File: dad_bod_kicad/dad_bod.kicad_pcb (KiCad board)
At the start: 2 copper layers, 98.5 x 71.3 mm, 136 parts, among them J1 Conn_01x01, J10 Conn_01x03_Male, J11 BNC5-J-P-GN-RA-BH2D, J12 USB4085-GF-A_REVA4, J13 Conn_01x03_Male, J14 Conn_01x03_Male, J2 Conn_01x01, J3 Conn_01x01, J4 Conn_01x01, J5 Conn_01x03_Male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

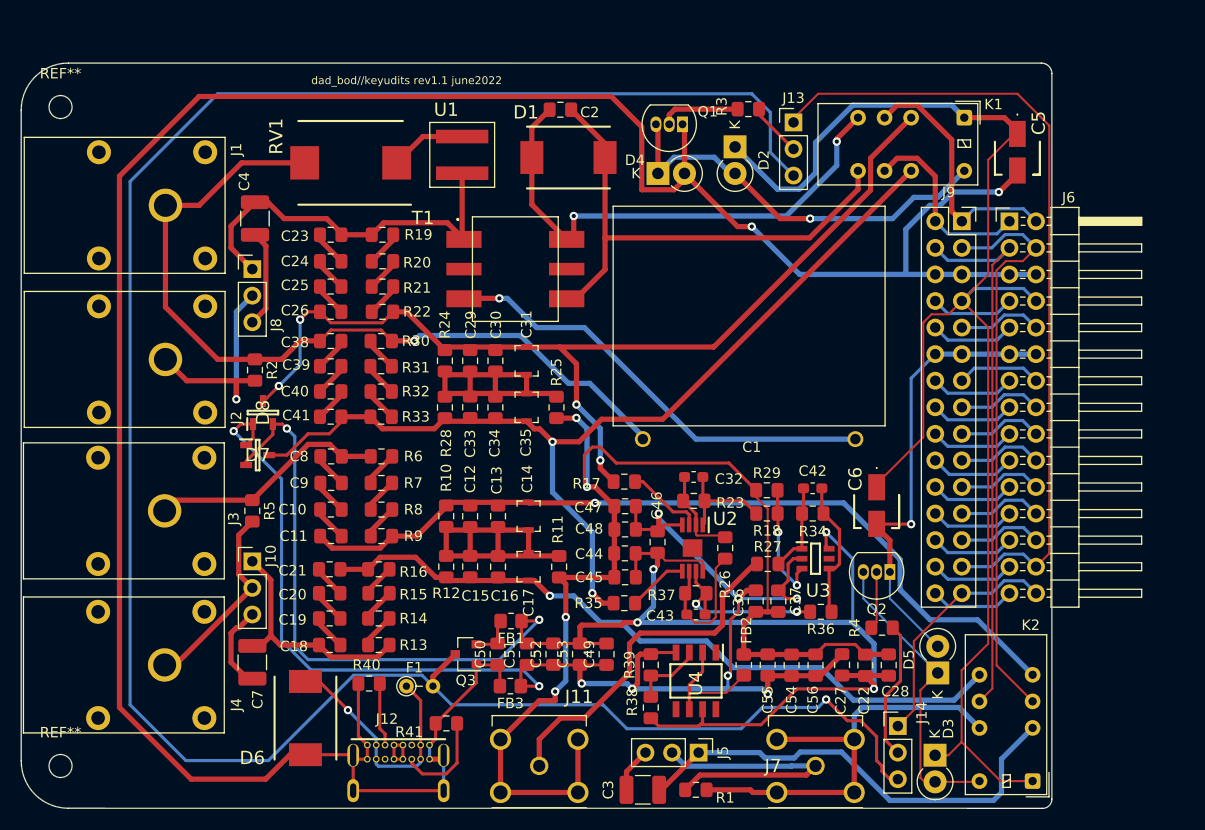
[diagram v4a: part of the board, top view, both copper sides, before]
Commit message: swapped div1 & div 2 inputs, bnc in can be routed as plc out
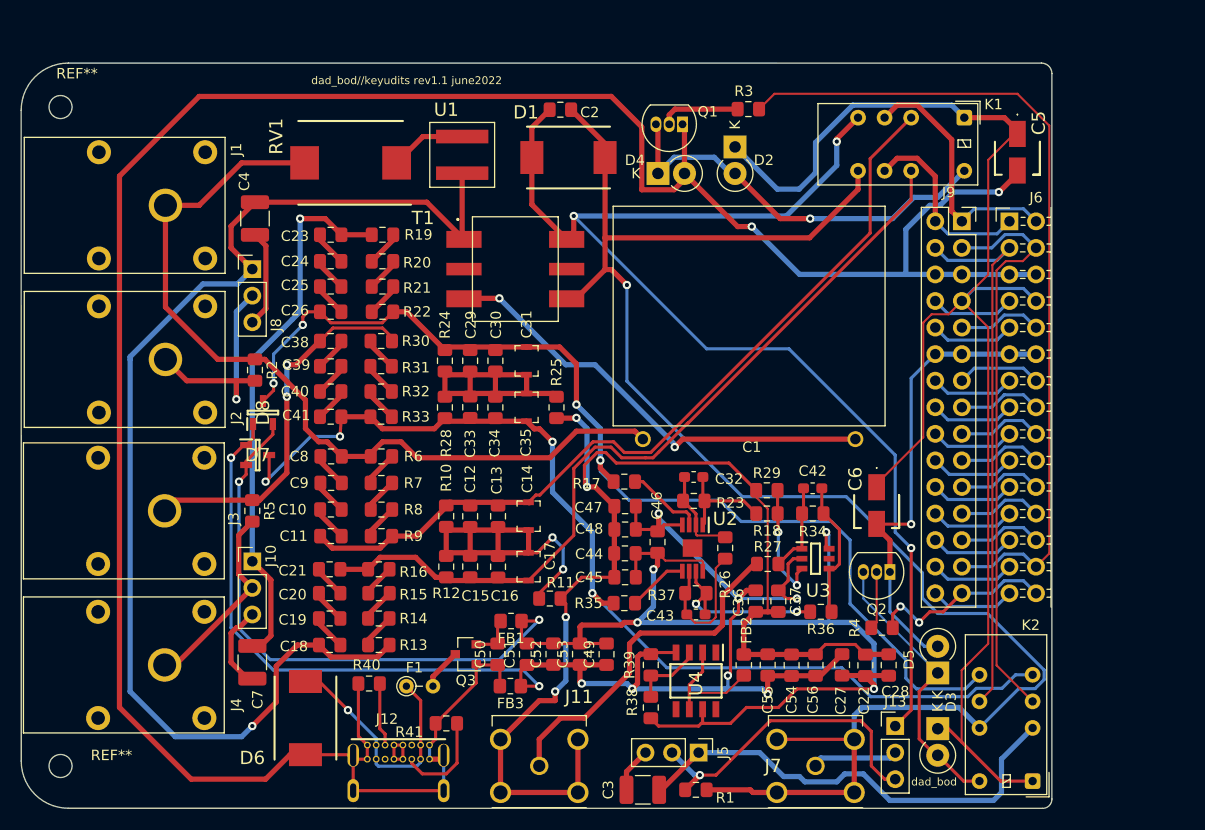
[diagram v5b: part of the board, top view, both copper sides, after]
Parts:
- removed J14: Conn_01x03_Male, Connector_PinHeader_2.54mm:PinHeader_1x03_P2.54mm_Vertical
- moved J13 58.5 mm to (130.3, 122.7)
- moved R11 3.17 mm to (97.3, 110.5), turned to 180 degrees
- moved D3 2.55 mm to (134.4, 122.9)
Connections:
- C1 pad 1: DIVin1- -> PLCin-
- C18 pad 1: DIVin2- -> PLCin+
- C4 pad 2: DIVin1+ -> PLCin+
- C7 pad 2: DIVin2- -> DIVin1+
- C8 pad 2: DIVin2+ -> PLCin-
- J1 pad 1: DIVin1- -> PLCin-
- J10 pad 1: DIVin2- -> DIVin1+
- J13 pad 1: CV6 -> PLCout+
- J13 pad 2: Net-(J13-Pad2) -> Net-(J7-Pad1)
- J13 pad 3: V+ -> bnc_imp+
- J3 pad 1: DIVin2+ -> DIVin1-
- J5 pad 2: Net-(J5-Pad2) -> bnc_imp+
- J7 pad 1: Net-(J5-Pad2) -> Net-(J7-Pad1)
- J7 pad 2: BNCin- -> PLCout-
- J7 pad 3: BNCin- -> PLCout-
- J7 pad 4: BNCin- -> PLCout-
- J7 pad 5: BNCin- -> PLCout-
- J8 pad 1: DIVin1+ -> PLCin+
- K1 pad 10: DIVout1- -> DIVout2-
- K1 pad 3: DIVout1+ -> DIVout2+
- K2 pad 10: BNCin- -> PLCout-
- K2 pad 5: DIVout2+ -> DIVout1-
- K2 pad 8: DIVout2- -> DIVout1+
- R1 pad 1: BNCin- -> PLCout-
- R1 pad 2: Net-(J5-Pad2) -> bnc_imp+
- R13 pad 2: DIVin2- -> PLCin+
- R2 pad 1: DIVin1- -> PLCin-
- R3 pad 1: Net-(J13-Pad2) -> CV6
- R4 pad 1: Net-(J14-Pad2) -> CV7
- R5 pad 1: DIVin2+ -> DIVin1-
- R6 pad 1: DIVin2+ -> PLCin-
- RV1 pad 2: DIVin1- -> PLCin-
- T1 pad 1: DIVin1+ -> PLCin+
- U1 pad 2: DIVin1+ -> PLCin+
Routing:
- net V+: track 213.4 -> 3.94 mm, vias 1 -> 0
- net PLCin+: track 0.00 -> 116.4 mm, vias 0 -> 1
- net PLCout-: track 49.3 -> 165.1 mm, vias 0 -> 1
- net PLCin-: track 0.00 -> 80.9 mm
- net PLCout+: track 49.6 -> 116.9 mm, vias 2 -> 3
- net DIVin1-: track 78.5 -> 35.8 mm, vias 1 -> 2
- net BNCin-: track 42.1 -> 0.00 mm
- net bnc_imp+: track 0.00 -> 30.6 mm, vias 0 -> 1
- net Net-(J5-Pad2): track 27.7 -> 0.00 mm
- net DIVin2+: track 22.8 -> 0.00 mm
- net DIVin2-: track 22.7 -> 0.00 mm
- net DIVin1+: track 37.1 -> 52.3 mm, vias 0 -> 1
- net Net-(J14-Pad2): track 13.3 -> 0.00 mm
- net DIVout2-: track 68.2 -> 78.4 mm, vias 1 -> 0
- net Net-(J7-Pad1): track 0.00 -> 8.29 mm
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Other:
- board text added: "dad_bod"

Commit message: touch ups & final review
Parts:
- moved J4 15.7 mm to (60.5, 101.1)
- moved J2 14.5 mm to (60.5, 73.2)
- moved J1 13.7 mm to (60.5, 86.6)
- moved J3 12.4 mm to (60.5, 114.6)
- moved REF** 0.51 mm to (50.5, 64.0)
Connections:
- K2 pad 5: DIVout1- -> DIVout1+
- K2 pad 8: DIVout1+ -> DIVout1-
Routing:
- net DIVin1-: track 35.8 -> 45.3 mm
- net DIVout1+: track 103.1 -> 109.3 mm
- net DIVout1-: track 101.7 -> 95.5 mm
- net Net-(J2-Pad1): track 21.7 -> 27.3 mm
- net relaypwr: track 138.5 -> 133.5 mm
- net Net-(J10-Pad2): track 18.9 -> 15.9 mm, vias 0 -> 1
- net GND: track 297.9 -> 295.4 mm
- net DIVin1+: track 52.3 -> 50.0 mm
- net Net-(D3-Pad2): track 30.8 -> 29.2 mm
- net PLCin+: track 116.4 -> 117.9 mm, vias 1 -> 2
- net Net-(C12-Pad1): track 36.6 -> 35.2 mm
- net Net-(D6-Pad1): track 23.8 -> 22.5 mm
- net Net-(C29-Pad1): track 27.9 -> 26.6 mm
- net greg: track 151.8 -> 150.8 mm
- net PLCout-: track 165.1 -> 164.2 mm
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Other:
- board size 98.5 x 71.3 mm -> 98.5 x 69.9 mm
- board text added: "dad_bod//keyudits rev1.2 july2022"
- board text removed: "dad_bod//keyudits rev1.1 june2022"
